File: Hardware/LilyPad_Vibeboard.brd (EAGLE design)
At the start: 20 x 20 mm, 10 parts, among them M1 MOTORSMD

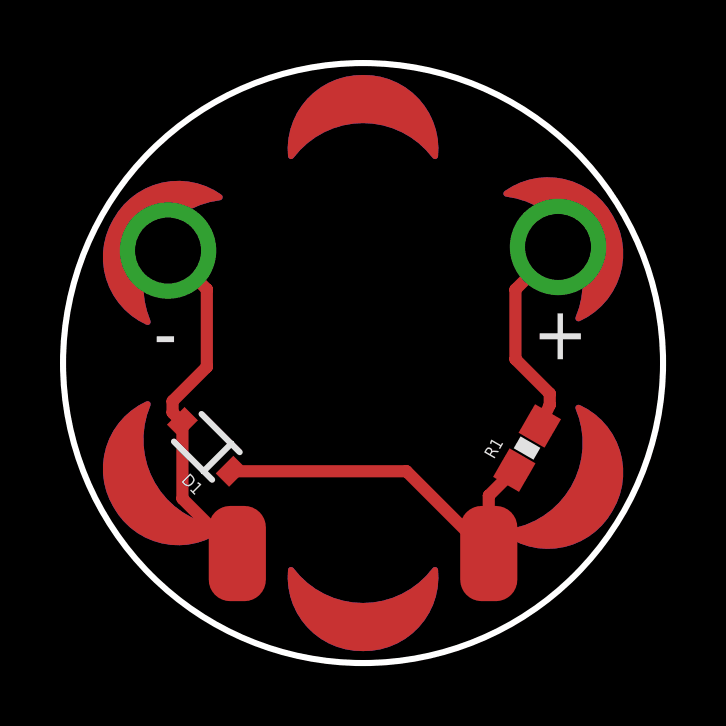
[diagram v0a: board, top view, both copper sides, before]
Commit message: Updated Schematic, Trace Routing added OSHW logo
Updated schematic to "frame letter"  re-routed previous traces that did
not pass the angle check, added OSHW logo.
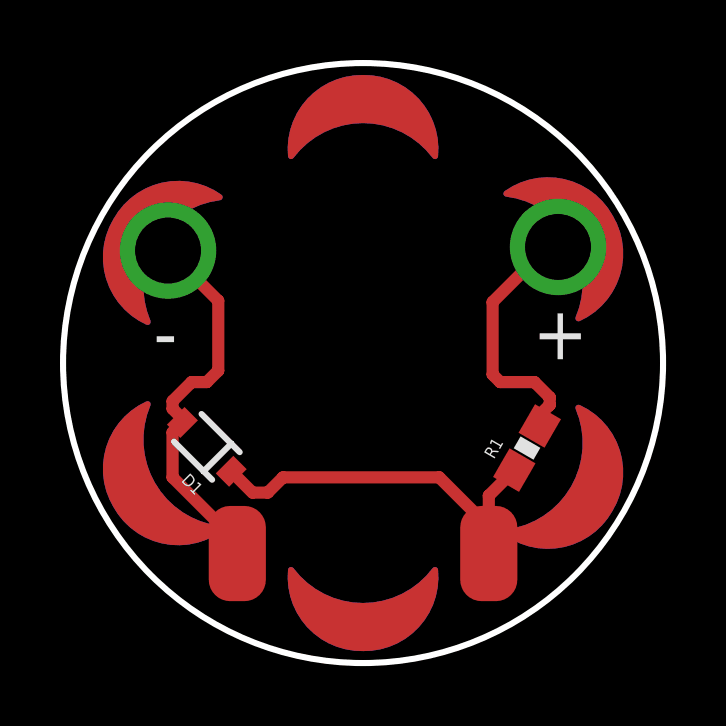
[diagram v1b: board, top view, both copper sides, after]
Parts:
- added FRAME1: FRAME-LETTER, SparkFun-Aesthetics:CREATIVE_COMMONS
- added LOGO1: OSHW-LOGOS, SparkFun-Aesthetics:OSHW-LOGO-S
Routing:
- net N$1: track 12.9 -> 13.8 mm
- net GND: track 12.0 -> 12.9 mm
- net 5V: track 7.47 -> 8.13 mm
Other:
- board text added: "Pete Lewis"
- board text added: "Revised by: Patrick Alberts"
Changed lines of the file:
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@@
 <layer number="144" name="Drill_legend" color="7" fill="1" visible="yes" active="yes"/>
 <layer number="151" name="HeatSink" color="7" fill="1" visible="yes" active="yes"/>
+<layer number="199" name="Contour" color="7" fill="1" visible="no" active="yes"/>
 <layer number="200" name="200bmp" color="1" fill="10" visible="no" active="no"/>
 <layer number="201" name="201bmp" color="2" fill="1" visible="no" active="no"/>
@@
 <vertex x="0" y="-9.851"/>
 </polygon>
+<text x="-68.58" y="0" size="1.778" layer="51" font="vector" ratio="10">Pete Lewis</text>
+<text x="-87.63" y="-2.54" size="1.778" layer="51" font="vector" ratio="10">Revised by: Patrick Alberts</text>
 </plain>
 <attributes>
@@
 </class>
 </classes>
-<designrules name="SparkFun">
+<designrules name="SparkFun *">
 <description language="en">&lt;b&gt;EAGLE Design Rules&lt;/b&gt;
 &lt;p&gt;
@@
 <param name="mdDrill" value="8mil"/>
 <param name="mdSmdStop" value="0mil"/>
-<param name="msWidth" value="8mil"/>
-<param name="msDrill" value="20mil"/>
+<param name="msWidth" value="7mil"/>
+<param name="msDrill" value="15mil"/>
 <param name="msMicroVia" value="9.99mm"/>
 <param name="msBlindViaRatio" value="0.5"/>
@@
 <param name="dpGapFactor" value="2.5"/>
 <param name="checkGrid" value="0"/>
-<param name="checkAngle" value="0"/>
+<param name="checkAngle" value="1"/>
 <param name="checkFont" value="1"/>
 <param name="checkRestrict" value="1"/>
@@
 <attribute name="VALUE" value="33k" x="5.466" y="-2.833" size="1.778" layer="27" rot="R60" display="off"/>
 </element>
+<element name="FRAME1" library="SparkFun-Aesthetics" package="CREATIVE_COMMONS" value="FRAME-LETTER" x="-98.88105625" y="0"/>
+<element name="LOGO1" library="SparkFun-Aesthetics" package="OSHW-LOGO-S" value="OSHW-LOGOS" x="0" y="3.81" rot="MR0"/>
 </elements>
 <signals>
@@
 <contactref element="D1" pad="1"/>
 <contactref element="R1" pad="1"/>
-<wire x1="4.191" y1="-6.35" x2="1.4481" y2="-3.6071" width="0.4064" layer="1"/>
-<wire x1="1.4481" y1="-3.6071" x2="-4.393825" y2="-3.607171875" width="0.4064" layer="1"/>
 <wire x1="4.191" y1="-6.35" x2="4.191" y2="-4.41911875" width="0.4064" layer="1"/>
 <wire x1="4.191" y1="-4.41911875" x2="5.041" y2="-3.56911875" width="0.4064" layer="1"/>
+<wire x1="4.191" y1="-6.35" x2="4.191" y2="-5.461" width="0.4064" layer="1"/>
+<wire x1="4.191" y1="-5.461" x2="2.54" y2="-3.81" width="0.4064" layer="1"/>
+<wire x1="2.54" y1="-3.81" x2="-2.667" y2="-3.81" width="0.4064" layer="1"/>
+<wire x1="-2.667" y1="-3.81" x2="-3.175" y2="-4.318" width="0.4064" layer="1"/>
+<wire x1="-3.175" y1="-4.318" x2="-3.682996875" y2="-4.318" width="0.4064" layer="1"/>
+<wire x1="-3.682996875" y1="-4.318" x2="-4.393825" y2="-3.607171875" width="0.4064" layer="1"/>
 </signal>
 <signal name="5V">
@@
 <contactref element="R1" pad="2"/>
 <wire x1="5.891" y1="-2.096878125" x2="5.891" y2="-1.729" width="0.4064" layer="1"/>
-<wire x1="6.223" y1="-1.397" x2="6.223" y2="-1.016" width="0.4064" layer="1"/>
-<wire x1="6.223" y1="-1.016" x2="5.08" y2="0.127" width="0.4064" layer="1"/>
-<wire x1="5.08" y1="0.127" x2="5.08" y2="2.45" width="0.4064" layer="1"/>
-<wire x1="5.08" y1="2.45" x2="6.5" y2="3.87" width="0.4064" layer="1"/>
-<wire x1="6.223" y1="-1.397" x2="5.891" y2="-2.096878125" width="0.4064" layer="1"/>
+<wire x1="5.891" y1="-1.729" x2="6.223" y2="-1.397" width="0.4064" layer="1"/>
+<wire x1="6.223" y1="-1.397" x2="6.223" y2="-1.143" width="0.4064" layer="1"/>
+<wire x1="6.223" y1="-1.143" x2="5.715" y2="-0.635" width="0.4064" layer="1"/>
+<wire x1="5.715" y1="-0.635" x2="4.572" y2="-0.635" width="0.4064" layer="1"/>
+<wire x1="4.572" y1="-0.635" x2="4.318" y2="-0.381" width="0.4064" layer="1"/>
+<wire x1="4.318" y1="-0.381" x2="4.318" y2="2.032" width="0.4064" layer="1"/>
+<wire x1="4.318" y1="2.032" x2="5.842" y2="3.556" width="0.4064" layer="1"/>
+<wire x1="5.842" y1="3.556" x2="6.096" y2="3.556" width="0.4064" layer="1"/>
+<wire x1="6.096" y1="3.556" x2="6.5" y2="3.87" width="0" layer="19" extent="1-1"/>
 </signal>
 <signal name="GND">
@@
 <contactref element="D1" pad="2"/>
 <contactref element="VIBE-" pad="1"/>
-<wire x1="-6.0201" y1="-4.5209" x2="-4.191" y2="-6.35" width="0.4064" layer="1"/>
-<wire x1="-6.020171875" y1="-1.980825" x2="-6.0201" y2="-4.5209" width="0.4064" layer="1"/>
-<wire x1="-6.020171875" y1="-1.980825" x2="-6.020175" y2="-1.980825" width="0.4064" layer="1"/>
-<wire x1="-6.020175" y1="-1.980825" x2="-6.35" y2="-1.651" width="0.4064" layer="1"/>
-<wire x1="-6.35" y1="-1.651" x2="-6.35" y2="-1.27" width="0.4064" layer="1"/>
-<wire x1="-6.35" y1="-1.27" x2="-5.207" y2="-0.127" width="0.4064" layer="1"/>
-<wire x1="-5.207" y1="-0.127" x2="-5.207" y2="2.457" width="0.4064" layer="1"/>
-<wire x1="-5.207" y1="2.457" x2="-6.5" y2="3.75" width="0.4064" layer="1"/>
+<wire x1="-6.020171875" y1="-1.980825" x2="-6.020171875" y2="-1.853828125" width="0.4064" layer="1"/>
+<wire x1="-6.020171875" y1="-1.853828125" x2="-6.35" y2="-1.524" width="0.4064" layer="1"/>
+<wire x1="-6.35" y1="-1.524" x2="-6.35" y2="-1.27" width="0.4064" layer="1"/>
+<wire x1="-6.35" y1="-1.27" x2="-5.715" y2="-0.635" width="0.4064" layer="1"/>
+<wire x1="-5.715" y1="-0.635" x2="-5.207" y2="-0.635" width="0.4064" layer="1"/>
+<wire x1="-5.207" y1="-0.635" x2="-4.826" y2="-0.254" width="0.4064" layer="1"/>
+<wire x1="-4.826" y1="-0.254" x2="-4.826" y2="2.076" width="0.4064" layer="1"/>
+<wire x1="-4.826" y1="2.076" x2="-6.5" y2="3.75" width="0.4064" layer="1"/>
+<wire x1="-4.191" y1="-6.35" x2="-4.191" y2="-5.969" width="0.4064" layer="1"/>
+<wire x1="-4.191" y1="-5.969" x2="-6.35" y2="-3.81" width="0.4064" layer="1"/>
+<wire x1="-6.35" y1="-3.81" x2="-6.35" y2="-2.310653125" width="0.4064" layer="1"/>
+<wire x1="-6.35" y1="-2.310653125" x2="-6.020171875" y2="-1.980825" width="0.4064" layer="1"/>
 </signal>
 </signals>

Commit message: Changed Silk
Moved posi/neg silk marks so that they can be clearly seen.
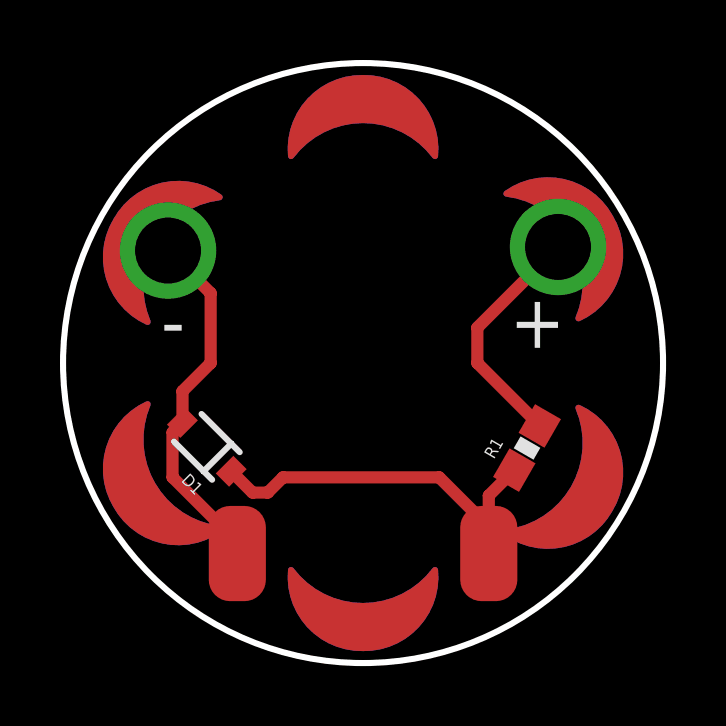
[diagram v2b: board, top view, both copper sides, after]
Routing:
- net GND: track 12.9 -> 12.1 mm
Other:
- board text added: "Leah Buechley"
- board text removed: "Pete Lewis"
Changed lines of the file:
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@@
 <layer number="18" name="Vias" color="2" fill="1" visible="yes" active="yes"/>
 <layer number="19" name="Unrouted" color="6" fill="1" visible="yes" active="yes"/>
-<layer number="20" name="Dimension" color="6" fill="1" visible="yes" active="yes"/>
+<layer number="20" name="Dimension" color="15" fill="1" visible="yes" active="yes"/>
 <layer number="21" name="tPlace" color="16" fill="1" visible="yes" active="yes"/>
 <layer number="22" name="bPlace" color="14" fill="1" visible="yes" active="yes"/>
@@
 <layer number="144" name="Drill_legend" color="7" fill="1" visible="yes" active="yes"/>
 <layer number="151" name="HeatSink" color="7" fill="1" visible="yes" active="yes"/>
-<layer number="199" name="Contour" color="7" fill="1" visible="no" active="yes"/>
+<layer number="199" name="Contour" color="7" fill="1" visible="yes" active="yes"/>
 <layer number="200" name="200bmp" color="1" fill="10" visible="no" active="no"/>
 <layer number="201" name="201bmp" color="2" fill="1" visible="no" active="no"/>
@@
 <circle x="0" y="0" radius="7.5" width="0.0508" layer="47"/>
 <circle x="0" y="0" radius="6.35" width="0.0508" layer="47"/>
-<text x="-6.985" y="0.127" size="1.778" layer="21" ratio="15">-</text>
-<text x="7.493" y="1.905" size="1.778" layer="21" ratio="15" rot="R180">+</text>
+<text x="-6.731" y="0.508" size="1.778" layer="21" ratio="15">-</text>
+<text x="6.731" y="2.286" size="1.778" layer="21" ratio="15" rot="R180">+</text>
 <polygon width="0.2032" layer="29">
 <vertex x="-6" y="0"/>
@@
 <vertex x="0" y="-9.851"/>
 </polygon>
-<text x="-68.58" y="0" size="1.778" layer="51" font="vector" ratio="10">Pete Lewis</text>
 <text x="-87.63" y="-2.54" size="1.778" layer="51" font="vector" ratio="10">Revised by: Patrick Alberts</text>
+<text x="-68.58" y="0" size="1.778" layer="51" font="vector" ratio="10">Leah Buechley</text>
 </plain>
 <attributes>
@@
 <contactref element="VIBE+" pad="1"/>
 <contactref element="R1" pad="2"/>
-<wire x1="5.891" y1="-2.096878125" x2="5.891" y2="-1.729" width="0.4064" layer="1"/>
-<wire x1="5.891" y1="-1.729" x2="6.223" y2="-1.397" width="0.4064" layer="1"/>
-<wire x1="6.223" y1="-1.397" x2="6.223" y2="-1.143" width="0.4064" layer="1"/>
-<wire x1="6.223" y1="-1.143" x2="5.715" y2="-0.635" width="0.4064" layer="1"/>
-<wire x1="5.715" y1="-0.635" x2="4.572" y2="-0.635" width="0.4064" layer="1"/>
-<wire x1="4.572" y1="-0.635" x2="4.318" y2="-0.381" width="0.4064" layer="1"/>
-<wire x1="4.318" y1="-0.381" x2="4.318" y2="2.032" width="0.4064" layer="1"/>
-<wire x1="4.318" y1="2.032" x2="5.842" y2="3.556" width="0.4064" layer="1"/>
-<wire x1="5.842" y1="3.556" x2="6.096" y2="3.556" width="0.4064" layer="1"/>
-<wire x1="6.096" y1="3.556" x2="6.5" y2="3.87" width="0" layer="19" extent="1-1"/>
+<wire x1="5.891" y1="-2.096878125" x2="5.891" y2="-2.081" width="0.4064" layer="1"/>
+<wire x1="5.891" y1="-2.081" x2="3.81" y2="0" width="0.4064" layer="1"/>
+<wire x1="3.81" y1="0" x2="3.81" y2="1.18" width="0.4064" layer="1"/>
+<wire x1="3.81" y1="1.18" x2="6.5" y2="3.87" width="0.4064" layer="1"/>
 </signal>
 <signal name="GND">
@@
 <contactref element="D1" pad="2"/>
 <contactref element="VIBE-" pad="1"/>
-<wire x1="-6.020171875" y1="-1.980825" x2="-6.020171875" y2="-1.853828125" width="0.4064" layer="1"/>
-<wire x1="-6.020171875" y1="-1.853828125" x2="-6.35" y2="-1.524" width="0.4064" layer="1"/>
-<wire x1="-6.35" y1="-1.524" x2="-6.35" y2="-1.27" width="0.4064" layer="1"/>
-<wire x1="-6.35" y1="-1.27" x2="-5.715" y2="-0.635" width="0.4064" layer="1"/>
-<wire x1="-5.715" y1="-0.635" x2="-5.207" y2="-0.635" width="0.4064" layer="1"/>
-<wire x1="-5.207" y1="-0.635" x2="-4.826" y2="-0.254" width="0.4064" layer="1"/>
-<wire x1="-4.826" y1="-0.254" x2="-4.826" y2="2.076" width="0.4064" layer="1"/>
-<wire x1="-4.826" y1="2.076" x2="-6.5" y2="3.75" width="0.4064" layer="1"/>
 <wire x1="-4.191" y1="-6.35" x2="-4.191" y2="-5.969" width="0.4064" layer="1"/>
 <wire x1="-4.191" y1="-5.969" x2="-6.35" y2="-3.81" width="0.4064" layer="1"/>
 <wire x1="-6.35" y1="-3.81" x2="-6.35" y2="-2.310653125" width="0.4064" layer="1"/>
 <wire x1="-6.35" y1="-2.310653125" x2="-6.020171875" y2="-1.980825" width="0.4064" layer="1"/>
+<wire x1="-6.020171875" y1="-1.980825" x2="-6.020171875" y2="-0.940171875" width="0.4064" layer="1"/>
+<wire x1="-6.020171875" y1="-0.940171875" x2="-5.08" y2="0" width="0.4064" layer="1"/>
+<wire x1="-5.08" y1="0" x2="-5.08" y2="2.33" width="0.4064" layer="1"/>
+<wire x1="-5.08" y1="2.33" x2="-6.5" y2="3.75" width="0.4064" layer="1"/>
 </signal>
 </signals>
